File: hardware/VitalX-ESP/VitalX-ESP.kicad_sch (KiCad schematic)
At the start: 56 parts, among them J1 ECG Probe, J2 GSR Probe, J3 UART, J4 JTAG, J5 Power terminal, Q1 BSS138, SW2 Reset, U1 AD8232ACPZ-R7, U3 ADP160AUJZ-1.8-R7, U4 ADPD144RI-ACEZ-RL, U5 AMS1117-3.3, U6 MCP601-xOT, U7 ESP32-S2-WROOM

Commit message: [nightly] Initial PCB layout.
4 layer stack up:
- Signal
- GND
- GND
- Signal
Currently working on ECG Block.
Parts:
- J1: footprint Connector_Audio:Jack_3.5mm_PJ320D_Horizontal -> AUDIO_SJ2-3593D-SMT-TR:SJ2-3593D-SMT-TR
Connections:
- net IN+: now also R1.1; no longer R1.2
- net LA: now also R1.2; no longer R1.1
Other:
- moved on the sheet: R1
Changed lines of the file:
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@@
       (effects (font (size 1.27 1.27)))
     )
-    (property "Footprint" "Connector_Audio:Jack_3.5mm_PJ320D_Horizontal" (at 40.005 198.755 0)
+    (property "Footprint" "AUDIO_SJ2-3593D-SMT-TR:SJ2-3593D-SMT-TR" (at 40.005 198.755 0)
       (effects (font (size 1.27 1.27)) hide)
     )
@@
     )
   )
-  (symbol (lib_id "Device:R") (at 88.265 216.535 90) (unit 1)
+  (symbol (lib_id "Device:R") (at 88.265 216.535 270) (mirror x) (unit 1)
     (in_bom yes) (on_board yes) (dnp no)
     (property "Reference" "R1" (at 88.265 212.09 90)

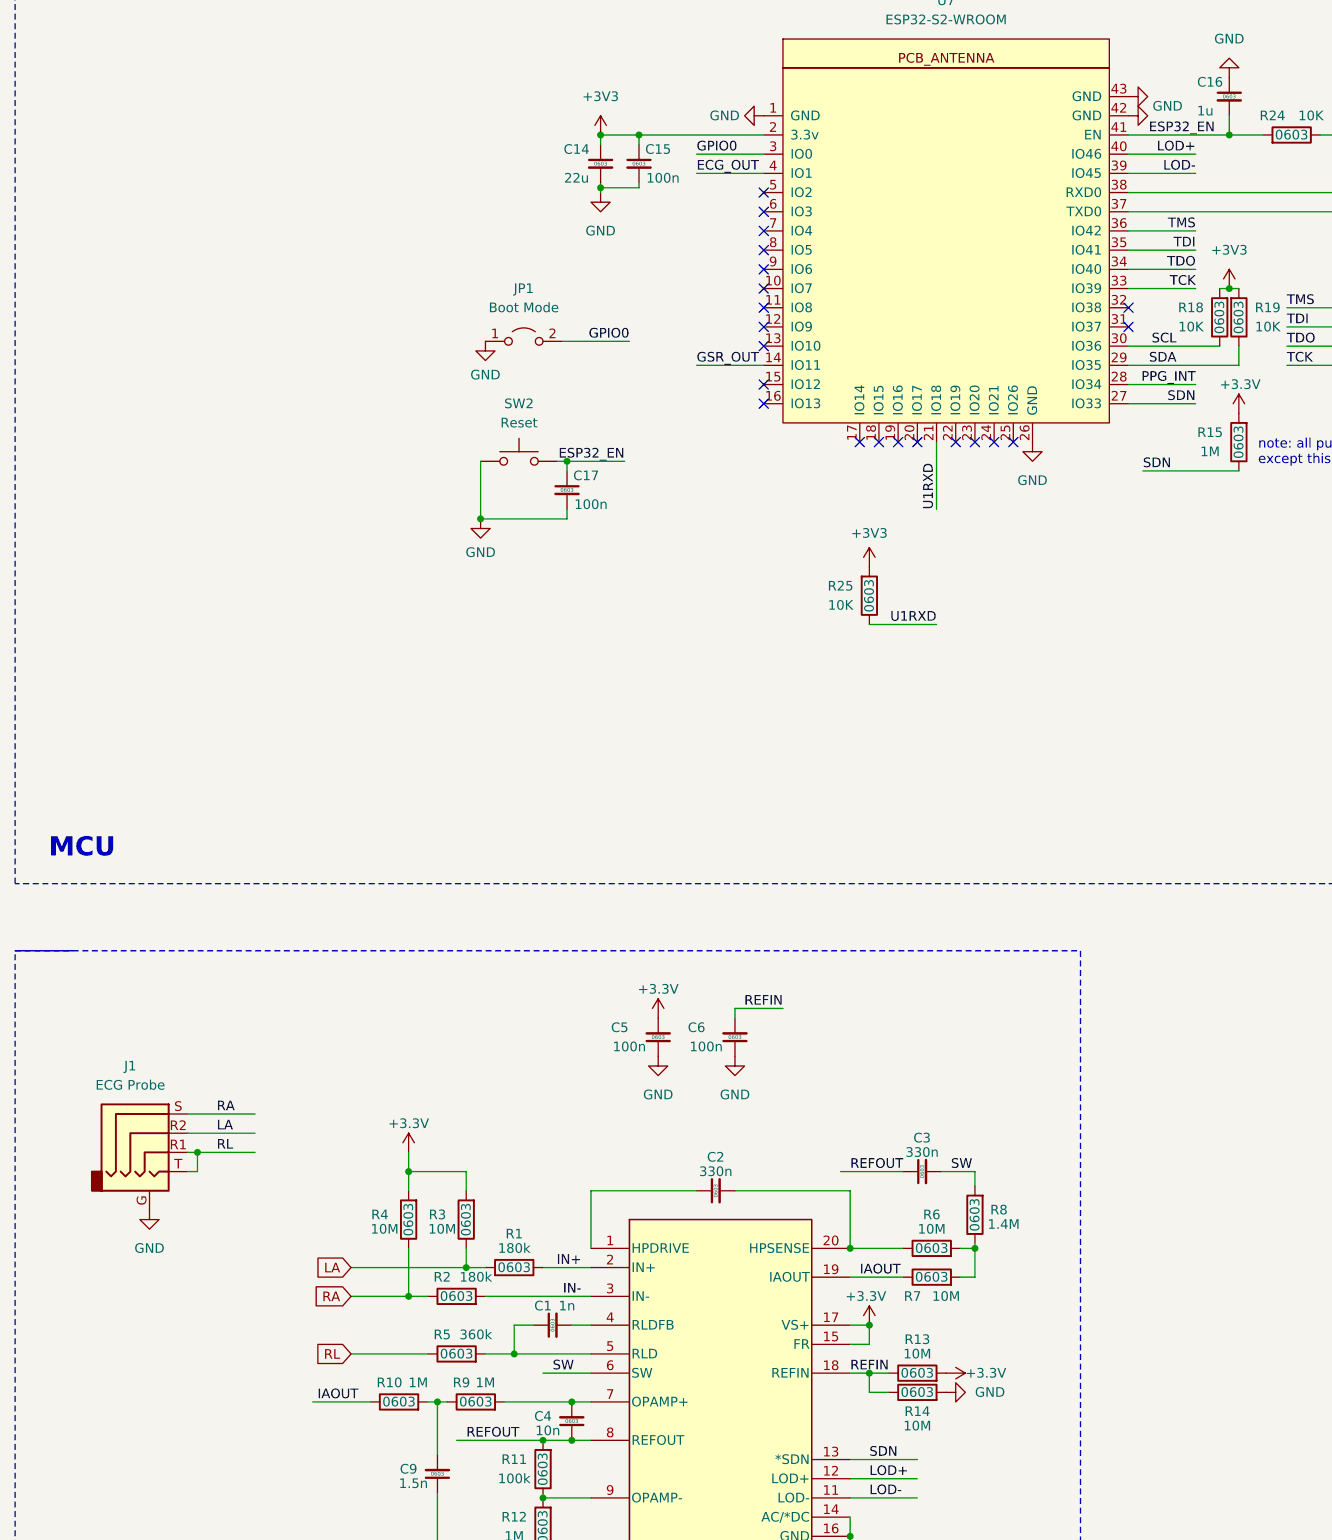
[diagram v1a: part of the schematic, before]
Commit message: [nightly] Change ECG Probe connector.
Utilized PJ-320D for ECG Probe connector.
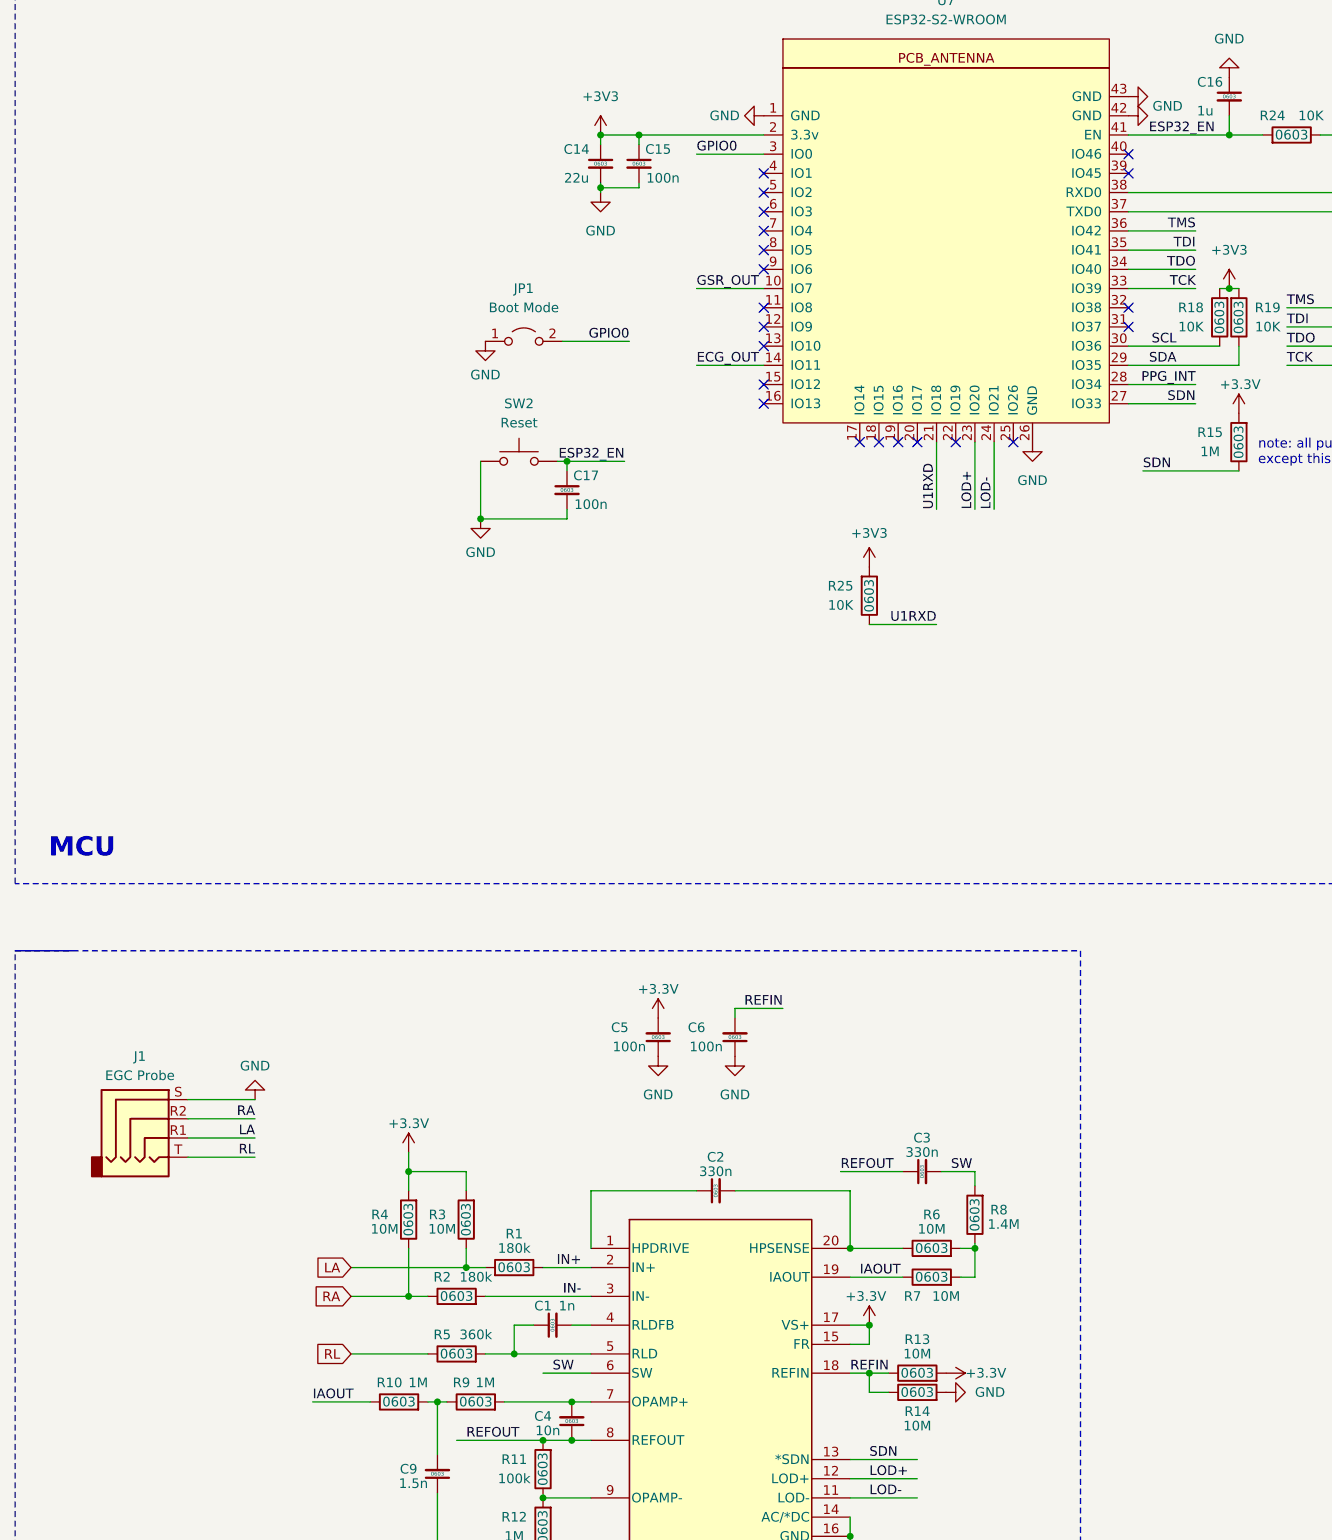
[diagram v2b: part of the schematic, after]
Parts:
- removed J1: ECG Probe, AUDIO_SJ2-3593D-SMT-TR:SJ2-3593D-SMT-TR, symbol Connector_Audio:AudioJack4_Ground
- added J1: EGC Probe, Connector_Audio:Jack_3.5mm_KoreanHropartsElec_PJ-320D-4A_Horizontal, symbol Connector_Audio:AudioJack4
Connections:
- net ECG_OUT: now also U7.14 (IO11); no longer U7.4 (IO1)
- net GND: now also J1.S
- net GSR_OUT: now also U7.10 (IO7); no longer U7.14 (IO11)
- net LA: now also J1.R1
- net LOD+: now also U7.23 (IO20); no longer U7.40 (IO46)
- net LOD-: now also U7.24 (IO21); no longer U7.39 (IO45)
- net RA: now also J1.R2
- net RL: now also J1.T
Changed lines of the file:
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@@
   (title_block
     (title "Vital X")
-    (date "2024-08-31")
+    (date "2024-09-04")
     (rev "Sample A")
   )
@@
   (junction (at 135.255 230.505) (diameter 0) (color 0 0 0 0)
   )
-  (junction (at 46.355 201.295) (diameter 0) (color 0 0 0 0)
-  )
   (junction (at 92.075 239.395) (diameter 0) (color 0 0 0 0)
   )
@@
   (junction (at 95.885 239.395) (diameter 0) (color 0 0 0 0)
   )
+  (no_connect (at 121.285 71.755))
   (no_connect (at 121.285 92.075))
+  (no_connect (at 169.545 71.755))
   (no_connect (at 357.505 109.855))
   (no_connect (at 121.285 76.835))
-  (no_connect (at 149.225 107.315))
   (no_connect (at 133.985 107.315))
   (no_connect (at 357.505 112.395))
@@
   (no_connect (at 141.605 107.315))
   (no_connect (at 121.285 81.915))
-  (no_connect (at 121.285 86.995))
   (no_connect (at 121.285 99.695))
   (no_connect (at 121.285 74.295))
@@
   (no_connect (at 121.285 79.375))
   (no_connect (at 139.065 107.315))
-  (no_connect (at 151.765 107.315))
   (no_connect (at 169.545 89.535))
   (no_connect (at 121.285 89.535))
   (no_connect (at 121.285 102.235))
+  (no_connect (at 169.545 69.215))
   (no_connect (at 154.305 107.315))
   (wire (pts (xy 132.715 230.505) (xy 135.255 230.505))
@@
     (stroke (width 0) (type default))
   )
-  (wire (pts (xy 353.695 194.31) (xy 353.695 198.12))
+  (wire (pts (xy 45.085 194.31) (xy 53.975 194.31))
     (stroke (width 0) (type default))
   )
-  (wire (pts (xy 95.25 117.475) (xy 95.25 116.205))
+  (wire (pts (xy 353.695 194.31) (xy 353.695 198.12))
     (stroke (width 0) (type default))
   )
-  (wire (pts (xy 45.085 203.835) (xy 46.355 203.835))
+  (wire (pts (xy 95.25 117.475) (xy 95.25 116.205))
     (stroke (width 0) (type default))
   )
@@
     (stroke (width 0) (type default))
   )
-  (wire (pts (xy 169.545 71.755) (xy 178.435 71.755))
+  (wire (pts (xy 151.765 107.315) (xy 151.765 116.205))
     (stroke (width 0) (type default))
   )
@@
     (stroke (width 0) (type default))
   )
-  (wire (pts (xy 45.085 201.295) (xy 46.355 201.295))
+  (wire (pts (xy 45.085 201.93) (xy 53.975 201.93))
     (stroke (width 0) (type default))
   )
@@
     (stroke (width 0) (type default))
   )
-  (wire (pts (xy 112.395 71.755) (xy 121.285 71.755))
+  (wire (pts (xy 112.395 86.995) (xy 121.285 86.995))
     (stroke (width 0) (type default))
   )
@@
     (stroke (width 0) (type default))
   )
-  (wire (pts (xy 45.085 196.215) (xy 53.975 196.215))
+  (wire (pts (xy 45.085 196.85) (xy 53.975 196.85))
     (stroke (width 0) (type default))
   )
@@
     (stroke (width 0) (type default))
   )
-  (wire (pts (xy 46.355 203.835) (xy 46.355 201.295))
-    (stroke (width 0) (type default))
-  )
   (wire (pts (xy 95.885 239.395) (xy 98.425 239.395))
     (stroke (width 0) (type default))
@@
     (stroke (width 0) (type default))
   )
-  (wire (pts (xy 46.355 201.295) (xy 53.975 201.295))
-    (stroke (width 0) (type default))
-  )
   (wire (pts (xy 199.39 89.535) (xy 190.5 89.535))
     (stroke (width 0) (type default))
@@
     (stroke (width 0) (type default))
   )
-  (wire (pts (xy 45.085 198.755) (xy 53.975 198.755))
+  (wire (pts (xy 45.085 199.39) (xy 53.975 199.39))
     (stroke (width 0) (type default))
   )
@@
     (stroke (width 0) (type default))
   )
-  (wire (pts (xy 169.545 69.215) (xy 178.435 69.215))
+  (wire (pts (xy 149.225 107.315) (xy 149.225 116.205))
     (stroke (width 0) (type default))
   )
@@
     (effects (font (size 1.27 1.27)) (justify right bottom))
   )
-  (label "ECG_OUT" (at 112.395 71.755 0) (fields_autoplaced)
+  (label "ECG_OUT" (at 112.395 97.155 0) (fields_autoplaced)
     (effects (font (size 1.27 1.27)) (justify left bottom))
   )
@@
     (effects (font (size 1.27 1.27)) (justify left bottom))
   )
-  (label "LOD-" (at 178.435 71.755 180) (fields_autoplaced)
-    (effects (font (size 1.27 1.27)) (justify right bottom))
+  (label "LOD-" (at 151.765 116.205 90) (fields_autoplaced)
+    (effects (font (size 1.27 1.27)) (justify left bottom))
   )
   (label "SDA" (at 311.785 117.475 0) (fields_autoplaced)
@@
     (effects (font (size 1.27 1.27)) (justify left bottom))
   )
-  (label "RA" (at 48.895 196.215 0) (fields_autoplaced)
-    (effects (font (size 1.27 1.27)) (justify left bottom))
+  (label "RA" (at 53.975 196.85 180) (fields_autoplaced)
+    (effects (font (size 1.27 1.27)) (justify right bottom))
   )
   (label "GPIO0" (at 103.505 93.98 180) (fields_autoplaced)
@@
     (effects (font (size 1.27 1.27)) (justify left bottom))
   )
-  (label "RL" (at 48.895 201.295 0) (fields_autoplaced)
-    (effects (font (size 1.27 1.27)) (justify left bottom))
+  (label "RL" (at 53.975 201.93 180) (fields_autoplaced)
+    (effects (font (size 1.27 1.27)) (justify right bottom))
   )
-  (label "GSR_OUT" (at 112.395 97.155 0) (fields_autoplaced)
+  (label "GSR_OUT" (at 112.395 86.995 0) (fields_autoplaced)
     (effects (font (size 1.27 1.27)) (justify left bottom))
   )
@@
     (effects (font (size 1.27 1.27)) (justify right bottom))
   )
-  (label "LOD+" (at 178.435 69.215 180) (fields_autoplaced)
-    (effects (font (size 1.27 1.27)) (justify right bottom))
+  (label "LOD+" (at 149.225 116.205 90) (fields_autoplaced)
+    (effects (font (size 1.27 1.27)) (justify left bottom))
   )
   (label "TMS" (at 178.435 79.375 180) (fields_autoplaced)
     (effects (font (size 1.27 1.27)) (justify right bottom))
   )
-  (label "IAOUT" (at 62.23 234.315 0) (fields_autoplaced)
+  (label "IAOUT" (at 61.595 234.315 0) (fields_autoplaced)
     (effects (font (size 1.27 1.27)) (justify left bottom))
   )
@@
     (effects (font (size 1.27 1.27)) (justify right bottom))
   )
-  (label "LA" (at 48.895 198.755 0) (fields_autoplaced)
-    (effects (font (size 1.27 1.27)) (justify left bottom))
+  (label "LA" (at 53.975 199.39 180) (fields_autoplaced)
+    (effects (font (size 1.27 1.27)) (justify right bottom))
   )
   (label "INT" (at 311.785 109.855 0) (fields_autoplaced)
     (effects (font (size 1.27 1.27)) (justify left bottom))
   )
-  (label "REFOUT" (at 132.715 203.835 0) (fields_autoplaced)
+  (label "REFOUT" (at 131.445 203.835 0) (fields_autoplaced)
     (effects (font (size 1.27 1.27)) (justify left bottom))
   )
@@
     )
   )
-  (symbol (lib_id "Connector_Audio:AudioJack4_Ground") (at 40.005 198.755 0) (unit 1)
-    (in_bom yes) (on_board yes) (dnp no) (fields_autoplaced)
-    (property "Reference" "J1" (at 37.465 189.865 0)
-      (effects (font (size 1.27 1.27)))
-    )
-    (property "Value" "ECG Probe" (at 37.465 192.405 0)
-      (effects (font (size 1.27 1.27)))
-    )
-    (property "Footprint" "AUDIO_SJ2-3593D-SMT-TR:SJ2-3593D-SMT-TR" (at 40.005 198.755 0)
-      (effects (font (size 1.27 1.27)) hide)
-    )
-    (property "Datasheet" "~" (at 40.005 198.755 0)
-      (effects (font (size 1.27 1.27)) hide)
-    )
-    (pin "G")
-    (pin "T")
-    (pin "R2")
-    (pin "R1")
-    (pin "S")
-    (instances
-      (project "VitalX-ESP"
-        (path "/c6ad7dc7-b487-4ed9-a043-5d3a4b3b13ea"
-          (reference "J1") (unit 1)
-        )
-      )
-    )
-  )
   (symbol (lib_id "power:GND") (at 169.545 61.595 90) (unit 1)
     (in_bom yes) (on_board yes) (dnp no)
@@
   )
   (symbol (lib_id "Connector_Generic:Conn_01x04") (at 204.47 74.295 0) (unit 1)
-    (in_bom yes) (on_board yes) (dnp no) (fields_autoplaced)
+    (in_bom yes) (on_board yes) (dnp no)
     (property "Reference" "J3" (at 207.01 74.295 0)
       (effects (font (size 1.27 1.27)) (justify left))
@@
     )
   )
+  (symbol (lib_id "Connector_Audio:AudioJack4") (at 40.005 196.85 0) (unit 1)
+    (in_bom yes) (on_board yes) (dnp no)
+    (property "Reference" "J1" (at 38.735 188.595 0)
+      (effects (font (size 1.27 1.27)))
+    )
+    (property "Value" "EGC Probe" (at 38.735 191.135 0)
+      (effects (font (size 1.27 1.27)))
+    )
+    (property "Footprint" "Connector_Audio:Jack_3.5mm_KoreanHropartsElec_PJ-320D-4A_Horizontal" (at 40.005 196.85 0)
+      (effects (font (size 1.27 1.27)) hide)
+    )
+    (property "Datasheet" "~" (at 40.005 196.85 0)
+      (effects (font (size 1.27 1.27)) hide)
+    )
+    (pin "R2")
+    (pin "S")
+    (pin "T")
+    (pin "R1")
+    (instances
+      (project "VitalX-ESP"
+        (path "/c6ad7dc7-b487-4ed9-a043-5d3a4b3b13ea"
+          (reference "J1") (unit 1)
+        )
+      )
+    )
+  )
   (symbol (lib_id "Device:C_Small") (at 117.475 186.055 180) (unit 1)
     (in_bom yes) (on_board yes) (dnp no)
@@
     )
   )
-  (symbol (lib_id "power:GND") (at 40.005 208.915 0) (unit 1)
+  (symbol (lib_id "power:GND") (at 53.975 194.31 180) (unit 1)
     (in_bom yes) (on_board yes) (dnp no) (fields_autoplaced)
-    (property "Reference" "#PWR05" (at 40.005 215.265 0)
+    (property "Reference" "#PWR05" (at 53.975 187.96 0)
       (effects (font (size 1.27 1.27)) hide)
     )
-    (property "Value" "GND" (at 40.005 213.995 0)
+    (property "Value" "GND" (at 53.975 189.865 0)
       (effects (font (size 1.27 1.27)))
     )
-    (property "Footprint" "" (at 40.005 208.915 0)
+    (property "Footprint" "" (at 53.975 194.31 0)
       (effects (font (size 1.27 1.27)) hide)
     )
-    (property "Datasheet" "" (at 40.005 208.915 0)
+    (property "Datasheet" "" (at 53.975 194.31 0)
       (effects (font (size 1.27 1.27)) hide)
     )
